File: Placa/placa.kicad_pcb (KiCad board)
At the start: 2 copper layers, 70 x 80 mm, 70 parts, among them IC1 ATMEGA328-A, P1 CONN_01X04, P10 CONN_01X02, P11 CONN_01X02, P2 CONN_01X02, P3 CONN_01X02, P4 CONN_01X01, P5 CONN_01X02, P6 CONN_01X01, P7 CONN_01X02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

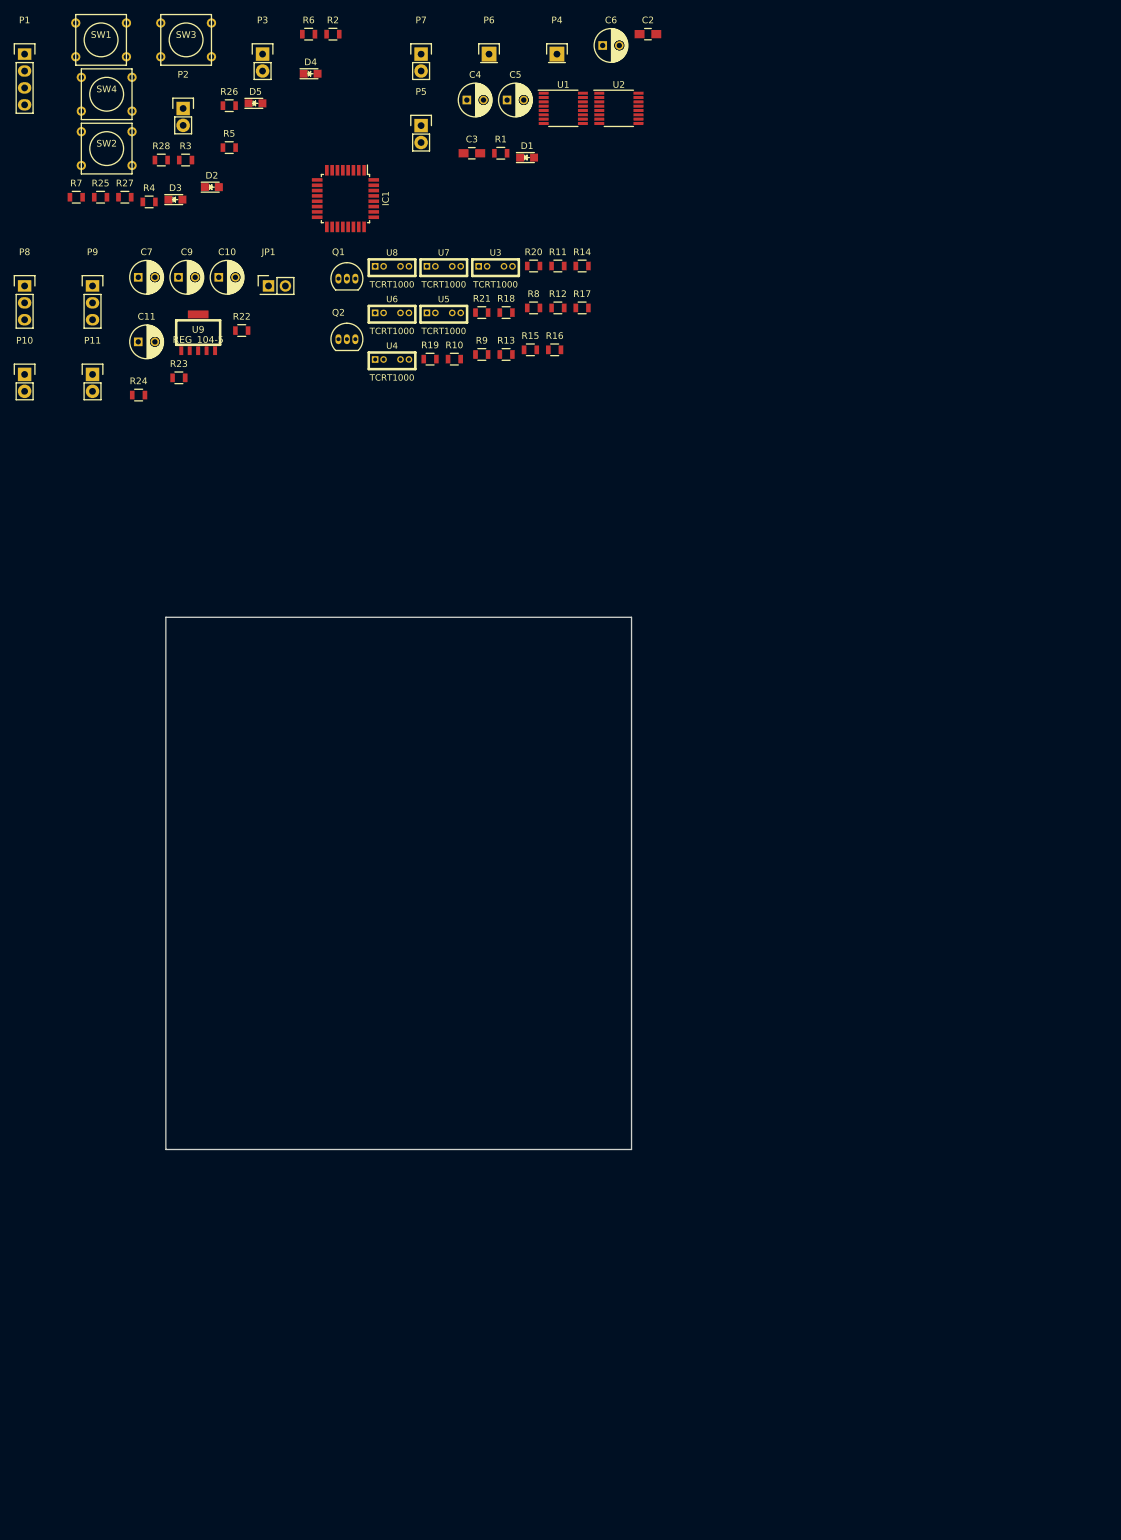
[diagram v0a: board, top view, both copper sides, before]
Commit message: Más avances en placa. Ignorados archivos bak.
Falta corregir algunas cosas en el esquemático, relacionado con los motores. El pcb está apenas empezado.
Se ignoraron los archivos bak y cache de kicad.
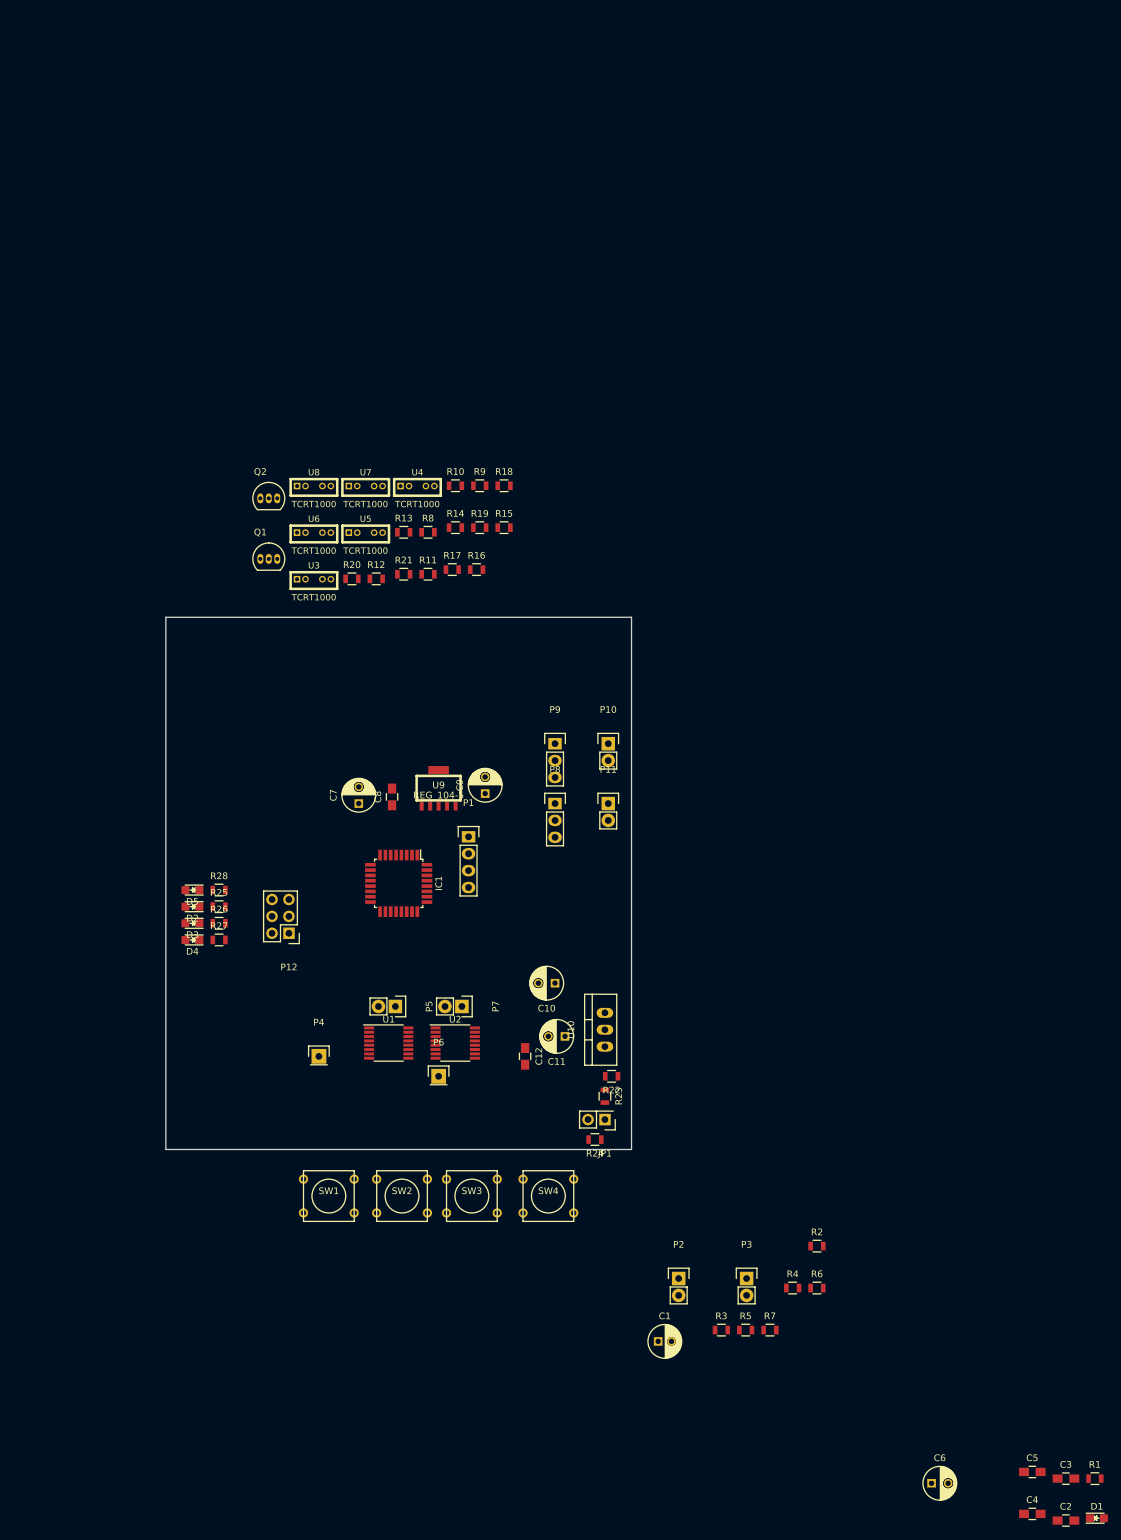
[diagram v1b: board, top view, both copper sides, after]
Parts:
- added C1: C, Capacitors_ThroughHole:C_Radial_D5_L11_P2, F.Cu at (174.0, 143.8)
- added C12: 0.1u, Capacitors_SMD:C_0805_HandSoldering, F.Cu at (154.0, 101.0)
- added C8: 0.1u, Capacitors_SMD:C_0805_HandSoldering, F.Cu at (134.0, 62.0)
- added P12: CONN_02X03, Pin_Headers:Pin_Header_Straight_2x03, F.Cu at (118.5, 82.5)
- added U10: LM1084IT-ADJ/NOPB, TO_SOT_Packages_THT:TO-220_Neutral123_Vertical, F.Cu at (166.0, 97.0)
- C4, C5: footprint Capacitors_ThroughHole:C_Radial_D5_L11_P2.5 -> Capacitors_SMD:C_0805_HandSoldering
- moved C2 232.1 mm to (235.3, 170.8)
- moved C4 228.9 mm to (230.2, 169.8)
- moved D1 221.7 mm to (239.9, 170.4)
- moved C6 221.7 mm to (215.1, 165.2)
- moved C5 220.8 mm to (230.2, 163.5)
- moved C3 218.3 mm to (235.3, 164.5)
- moved R1 218.3 mm to (239.6, 164.5)
- moved R6 203.4 mm to (197.9, 135.8)
- moved R7 199.7 mm to (190.8, 142.1)
- moved P3 197.9 mm to (187.3, 134.4)
- moved R2 196.2 mm to (197.9, 129.5)
- moved R5 194.0 mm to (187.2, 142.1)
- moved R3 193.4 mm to (183.5, 142.1)
- moved P2 191.0 mm to (177.1, 134.4)
- moved R4 189.8 mm to (194.2, 135.8)
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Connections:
- IC1 pad 11: /Led2 -> /Sensores/Habilitador2
- IC1 pad 12: /Led3 -> /Boton1
- IC1 pad 15: /Sensores/Habilitador1 -> /Led1
- IC1 pad 16: /Sensores/Habilitador2 -> /Led2
- IC1 pad 17: /Boton1 -> /Led3
- IC1 pad 2: /Led1 -> /Sensores/Habilitador1

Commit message: estan casi todas las cosas en su lugar, falta cambiar DVRs y regulador y rutear
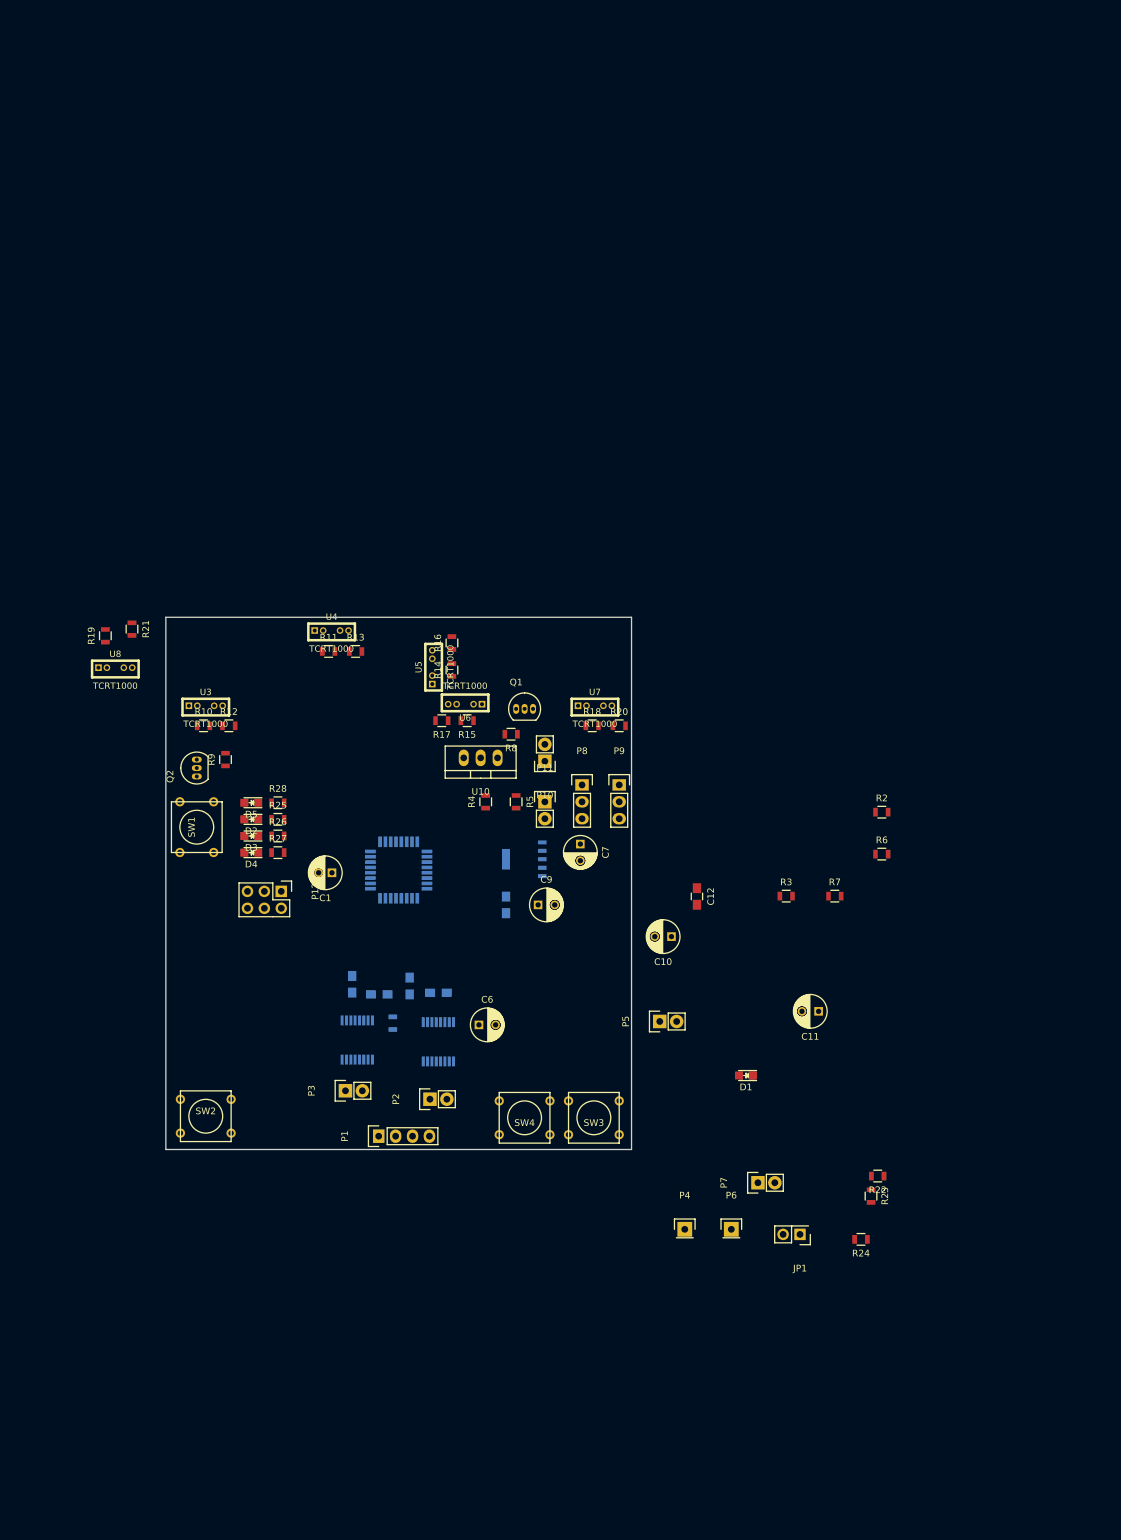
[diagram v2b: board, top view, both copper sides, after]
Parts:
- C2, C3, C4, C5, C8, IC1, R1, U1, U2, U9: moved to B.Cu
- moved C3 130.5 mm to (128.0, 90.2), turned to 90 degrees
- moved C2 127.2 mm to (136.7, 90.4), turned to 270 degrees
- moved R1 125.8 mm to (134.1, 96.0), turned to 270 degrees
- moved C5 121.6 mm to (132.1, 91.7), turned to 180 degrees
- moved C4 118.8 mm to (141.0, 91.4), turned to 180 degrees
- moved C6 96.8 mm to (147.1, 96.3)
- moved R5 86.6 mm to (152.7, 62.7), turned to 270 degrees
- moved R4 86.4 mm to (148.1, 62.7), turned to 90 degrees
- moved C1 85.8 mm to (125.0, 73.4), turned to 180 degrees
- moved D1 84.9 mm to (187.2, 103.9), turned to 180 degrees
- moved P3 66.6 mm to (127.0, 106.2), turned to 90 degrees
- moved R2 66.0 mm to (207.6, 64.3)
- moved R3 66.0 mm to (193.3, 76.9)
- moved R7 66.0 mm to (200.6, 76.9)
- moved R6 66.0 mm to (207.6, 70.6)
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
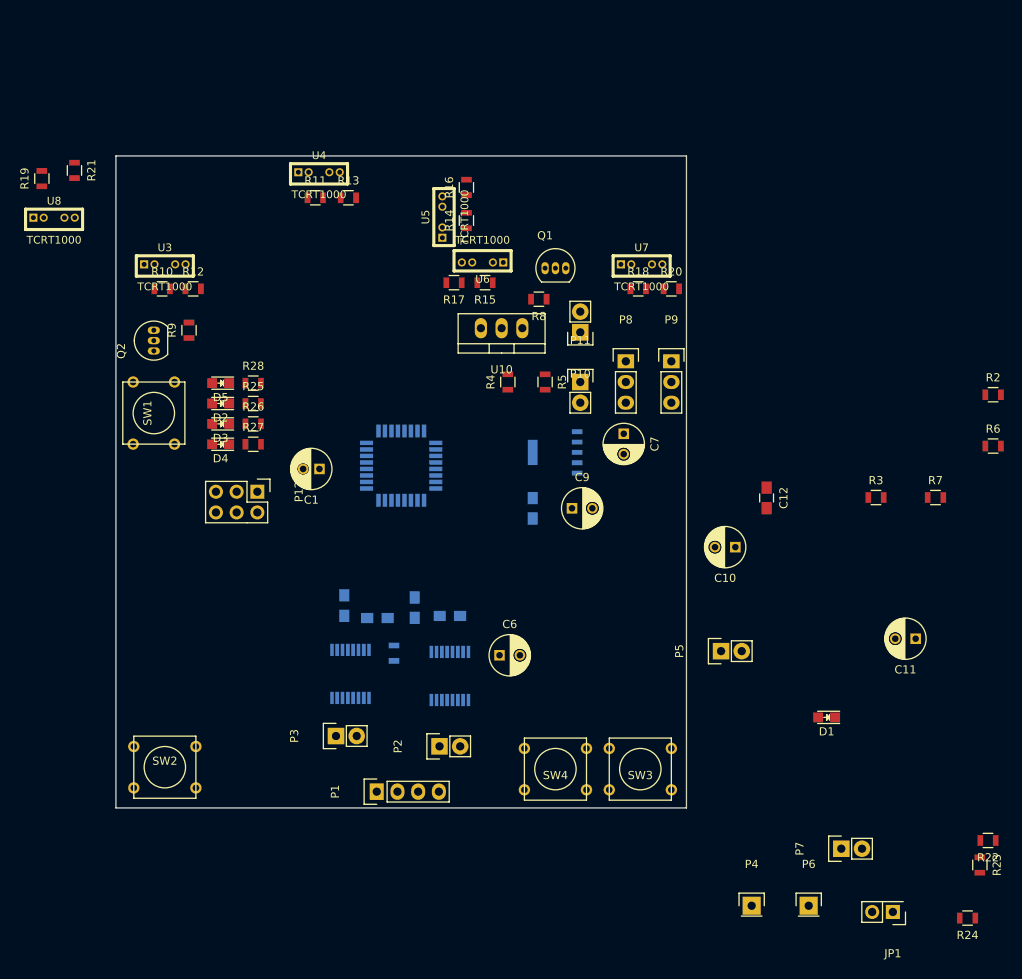
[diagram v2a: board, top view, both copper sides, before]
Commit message: se termino el esquematico y asociacion de componentes, falta acomodar y rutear PCB
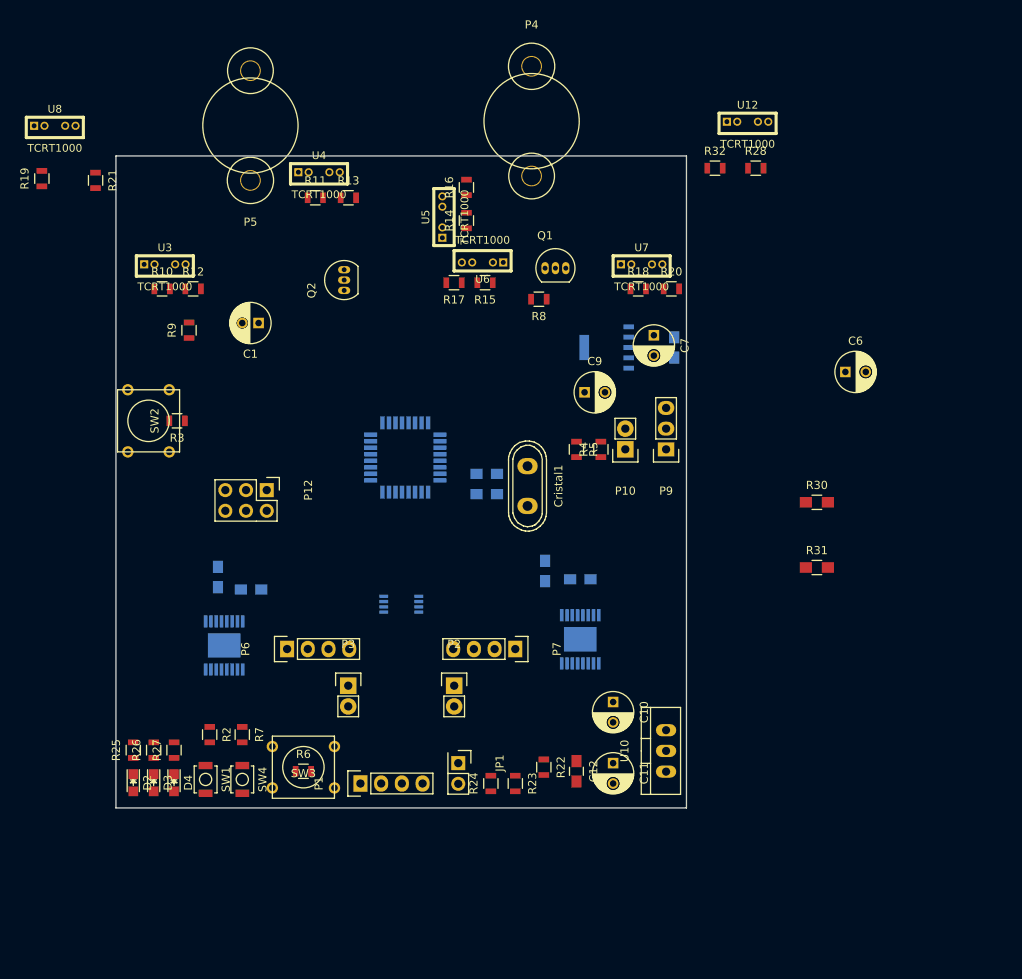
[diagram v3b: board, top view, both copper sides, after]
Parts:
- removed D1, D5: LED, LEDs:LED_0805
- removed P11: CONN_01X02, Pin_Headers:Pin_Header_Straight_1x02
- removed P8: CONN_01X03, Pin_Headers:Pin_Header_Straight_1x03
- removed R1: 1k, Resistors_SMD:R_0805
- added Cristal1: Crystal, Crystals:Crystal_HC50-U_Vertical, F.Cu at (150.5, 75.5)
- added Cxtal1: 22p, Capacitors_SMD:C_0805_HandSoldering, B.Cu at (145.5, 74.0)
- added Cxtal2: 22p, Capacitors_SMD:C_0805_HandSoldering, B.Cu at (145.5, 76.5)
- added R30: 47k, Resistors_SMD:R_0805_HandSoldering, F.Cu at (186.0, 77.5)
- added R31: 47k, Resistors_SMD:R_0805_HandSoldering, F.Cu at (186.0, 85.5)
- added R32: 33k, Resistors_SMD:R_0805, F.Cu at (173.5, 36.5)
- added U11: sn74lvc2g86, Housings_SSOP:TSSOP-8_3x3mm_Pitch0.65mm, B.Cu at (135.0, 90.0)
- added U12: TCRT1000, tcrt1000:TCRT1000, F.Cu at (177.5, 31.0)
- C8: value 0.1u -> 100n
- P4: value CONN_01X01 -> BallCaster2; footprint Pin_Headers:Pin_Header_Straight_1x01 -> ballcaster:Pin_Header_Straight_1x02
- P5: value CONN_01X02 -> BallCaster1; footprint Pin_Headers:Pin_Header_Straight_1x02 -> ballcaster:Pin_Header_Straight_1x02
- P6: value CONN_01X01 -> CONN_01X04; footprint Pin_Headers:Pin_Header_Straight_1x01 -> Pin_Headers:Pin_Header_Straight_1x04
- P7: value CONN_01X02 -> CONN_01X04; footprint Pin_Headers:Pin_Header_Straight_1x02 -> Pin_Headers:Pin_Header_Straight_1x04
- R28: value 220 -> 180
- R8, R9: value R -> 2k2
- SW1, SW4: footprint Buttons_Switches_ThroughHole:SW_PUSH_SMALL -> Buttons_Switches_SMD:SW_SPST_B3U-1000P
- U1, U2: footprint Housings_SSOP:TSSOP-16_4.4x5mm_Pitch0.65mm -> Bibliotecas:TSSOP-16_4.4x5mm_Pitch0.65mm
- moved P4 106.5 mm to (151.0, 24.0)
- moved R2 104.8 mm to (111.5, 106.0), turned to 270 degrees
- moved R6 93.6 mm to (123.0, 110.5)
- moved R7 89.9 mm to (115.5, 106.0), turned to 270 degrees
- moved R3 86.3 mm to (107.5, 67.5), turned to 180 degrees
- moved P5 81.7 mm to (116.5, 38.0), turned to 180 degrees
- moved P6 71.3 mm to (121.0, 95.5), turned to 90 degrees
- moved R28 67.1 mm to (178.5, 36.5)
- moved R24 60.8 mm to (146.0, 112.0), turned to 90 degrees
- moved R23 57.9 mm to (149.0, 112.0)
- moved JP1 56.4 mm to (142.0, 109.5), turned to 270 degrees
- moved U10 55.7 mm to (167.5, 108.0), turned to 90 degrees
- moved R22 55.2 mm to (152.5, 110.0), turned to 270 degrees
- moved C6 54.9 mm to (189.5, 61.5)
- moved D2 47.7 mm to (102.1, 111.9), turned to 270 degrees
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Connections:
- C10 pad 1: /Alimentacion/Vreg -> /Alimentacion/Vbat
- C9 pad 1: +8V -> /Alimentacion/Vbat
- IC1 pad 1: /Motores/M2VINT -> /EncoderM2
- IC1 pad 10: /Motores/M1IN1 -> /Motores/M2IN2
- IC1 pad 11: /Sensores/Habilitador2 -> /Boton2
- IC1 pad 14: /Motores/M2IN2 -> /Motores/M1IN1
- IC1 pad 2: /Sensores/Habilitador1 -> /Sensores/Habilitador
- IC1 pad 28: /Led4 -> /Sensores/Sensor7
- IC1 pad 31: /TX -> /BotonExtra
- IC1 pad 32: /Motores/M1VINT -> /EncoderM1
- IC1 pad 7: /Boton2 -> /XTAL1
- IC1 pad 8: /Boton3 -> /XTAL2
- P1 pad 2: /TX -> /BotonExtra
- P4 pad 1: Net-(P4-Pad1) -> (no net)
- P5 pad 1: VPP -> (no net)
- P5 pad 2: Net-(P5-Pad2) -> (no net)
- P6 pad 1: Net-(P6-Pad1) -> GND
- P7 pad 1: VPP -> GND
- P9 pad 3: +8V -> /Alimentacion/Vbat
- R28 pad 2: /Led4 -> GND
- R4 pad 1: +8V -> +BATT
- R7 pad 2: /Boton3 -> /BotonExtra
- R8 pad 2: /Sensores/Habilitador1 -> /Sensores/Habilitador
- R9 pad 2: /Sensores/Habilitador2 -> /Sensores/Habilitador
- SW4 pad 1: /Boton3 -> /BotonExtra
- U1 pad 1: Net-(P5-Pad2) -> Net-(R30-Pad1)
- U1 pad 8: Net-(P4-Pad1) -> (no net)
- U10 pad 3: /Alimentacion/Vreg -> /Alimentacion/Vbat
- U2 pad 1: Net-(P7-Pad2) -> Net-(R31-Pad1)
- U2 pad 8: Net-(P6-Pad1) -> (no net)
- U9 pad 1: +8V -> /Alimentacion/Vbat
- U9 pad 5: +8V -> /Alimentacion/Vbat
